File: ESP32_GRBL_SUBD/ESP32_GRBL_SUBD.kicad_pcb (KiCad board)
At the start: 2 copper layers, 67 x 91 mm, 44 parts, among them J1 DB25_Female_MountingHoles, J2 Micro_SD_Card, J3 Conn_01x19_Female, J3a1 Conn_01x19_Female, J4 Conn_01x19_Female, J4a1 Conn_01x19_Female, J5 Barrel_Jack_MountingPin, J6 Screw_Terminal_01x02, J7 Screw_Terminal_01x02, J8 Screw_Terminal_01x02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

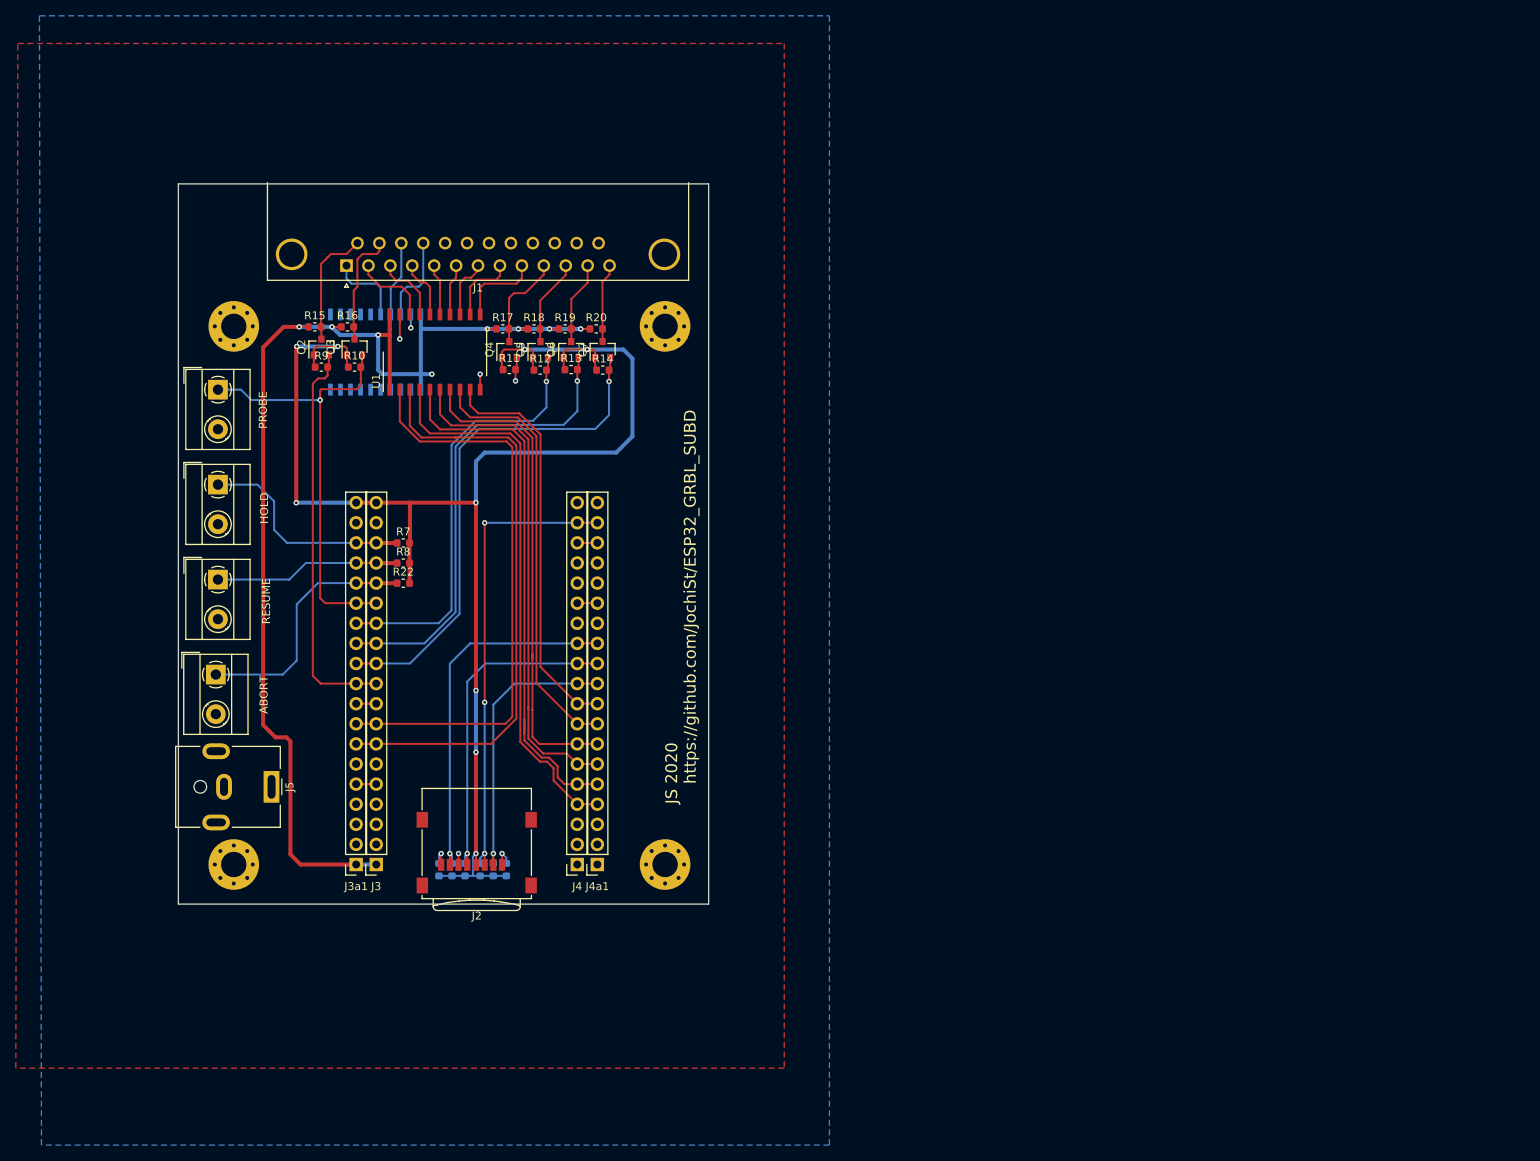
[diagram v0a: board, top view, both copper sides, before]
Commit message: added resistors to map outputs to different pins on SUB-D
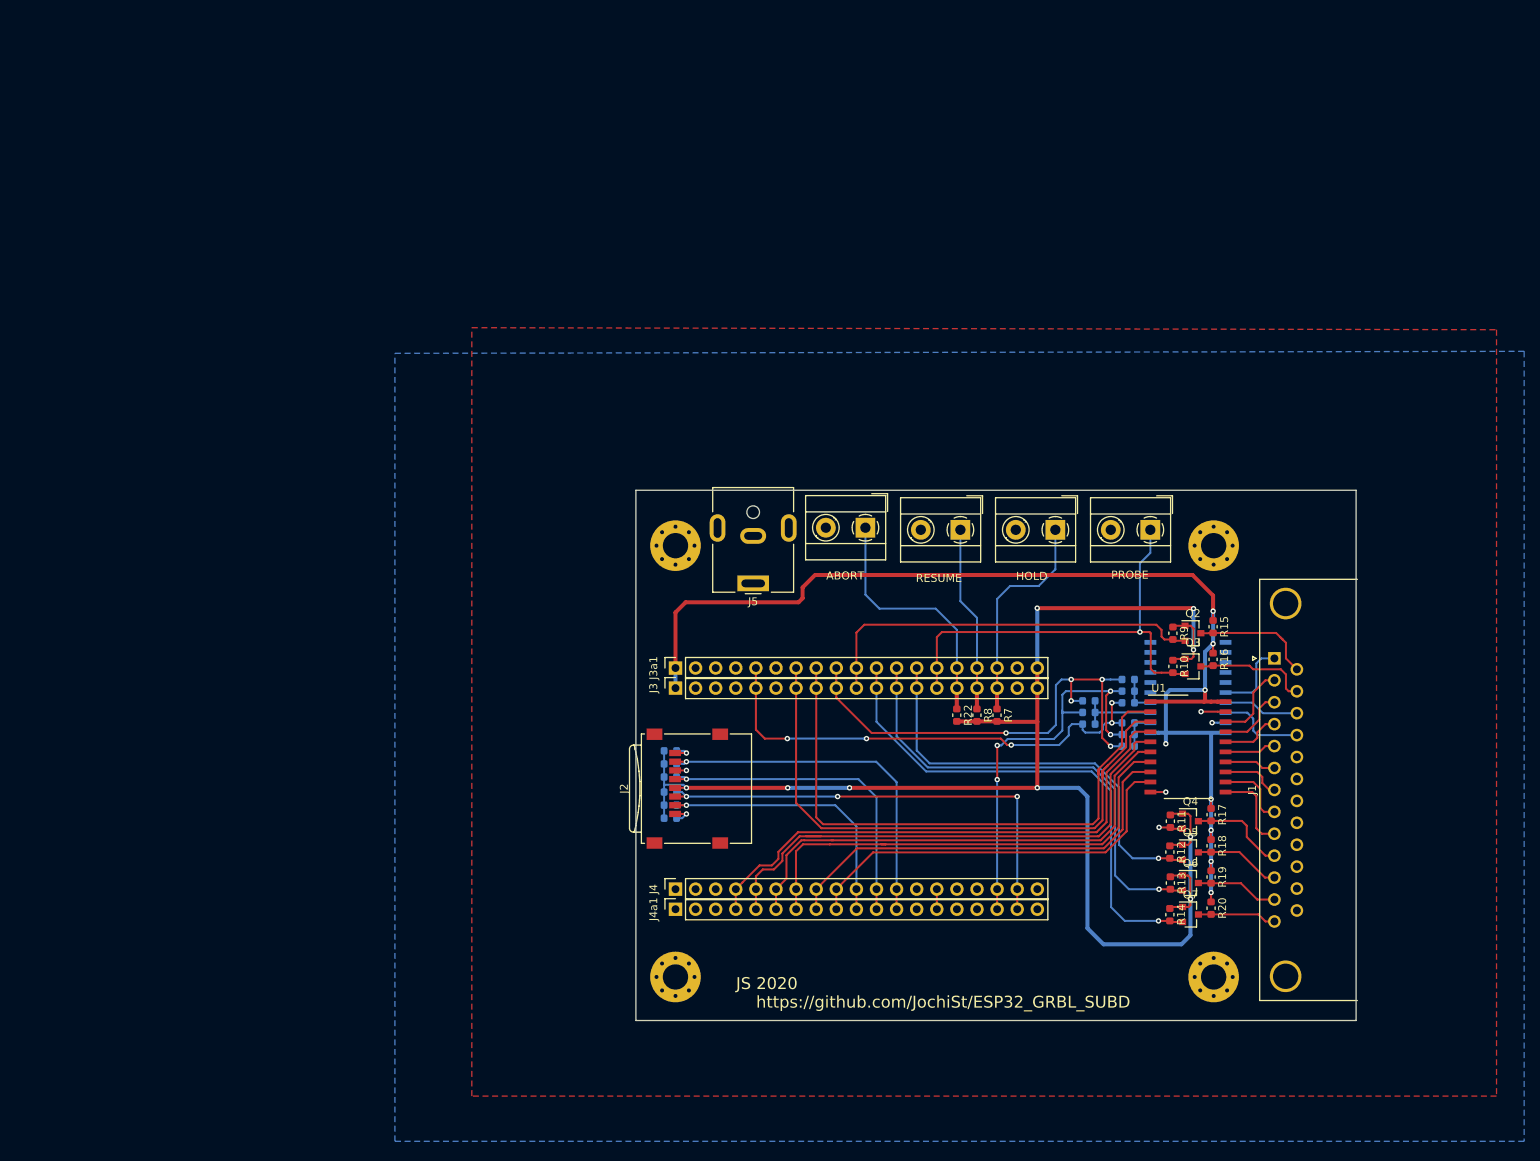
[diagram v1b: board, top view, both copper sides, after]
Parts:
- added R21: 0R, Resistor_SMD:R_0603_1608Metric, B.Cu at (138.0, 96.6)
- added R23: 0R, Resistor_SMD:R_0603_1608Metric, B.Cu at (138.0, 98.1)
- added R24: 0R, Resistor_SMD:R_0603_1608Metric, B.Cu at (138.0, 99.6)
- added R25: 0R, Resistor_SMD:R_0603_1608Metric, B.Cu at (133.0, 99.3)
- added R26: 0R, Resistor_SMD:R_0603_1608Metric, B.Cu at (133.0, 100.8)
- added R27: 0R, Resistor_SMD:R_0603_1608Metric, B.Cu at (133.0, 102.3)
- added R28: 0R, Resistor_SMD:R_0603_1608Metric, B.Cu at (138.0, 105.1)
- added R29: 0R, Resistor_SMD:R_0603_1608Metric, B.Cu at (138.0, 103.6)
- added R30: 0R, Resistor_SMD:R_0603_1608Metric, B.Cu at (138.0, 102.1)
- moved J1 127.3 mm to (156.5, 94.0), turned to 90 degrees
- moved H3 126.9 mm to (148.8, 79.7), turned to 270 degrees
- moved R15 119.7 mm to (148.7, 90.0), turned to 270 degrees
- moved J6 119.1 mm to (140.8, 77.7), turned to 180 degrees
- moved R16 117.2 mm to (148.7, 94.1), turned to 270 degrees
- moved Q2 115.9 mm to (146.2, 90.8), turned to 0 degrees
- moved Q3 113.4 mm to (146.2, 95.0), turned to 0 degrees
- moved R9 112.7 mm to (143.7, 90.8), turned to 270 degrees
- moved U2 111.1 mm to (145.6, 97.6), turned to 0 degrees
- moved R10 110.1 mm to (143.7, 95.0), turned to 270 degrees
- moved R17 108.5 mm to (148.5, 113.7), turned to 270 degrees
- moved R18 107.6 mm to (148.5, 117.6), turned to 270 degrees
- moved H2 107.5 mm to (148.8, 134.2), turned to 270 degrees
- moved U1 107.4 mm to (145.6, 105.1), turned to 0 degrees
- moved R19 107.0 mm to (148.5, 121.6), turned to 270 degrees
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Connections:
- U2 pad 5: Net-(U2-Pad5) -> GND
- U2 pad 6: Net-(U2-Pad6) -> GND
- U2 pad 7: Net-(U2-Pad7) -> GND
- U2 pad 8: /MIST_3V3 -> GND
- U2 pad 9: /FLOOD_3V3 -> GND
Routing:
- net /COOLANT_3V3: track 2.54 -> 62.1 mm, vias 0 -> 5
- net /STEP_ENABLE: track 2.54 -> 62.0 mm, vias 0 -> 5
- net /Spindle_EN_3V3: track 2.54 -> 51.9 mm, vias 0 -> 4
- net /ENABLE_3V3: track 0.00 -> 9.93 mm
- net /OUT2_3V3: track 0.00 -> 4.96 mm
- net /OUT1_3V3: track 0.00 -> 4.96 mm
- net /Y_DIR_3V3: track 69.6 -> 68.3 mm
- net /Y_STEP_3V3: track 68.9 -> 67.7 mm
- net /Z_DIR_3V3: track 63.7 -> 62.7 mm
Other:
- board size 67 x 91 mm -> 91 x 67 mm

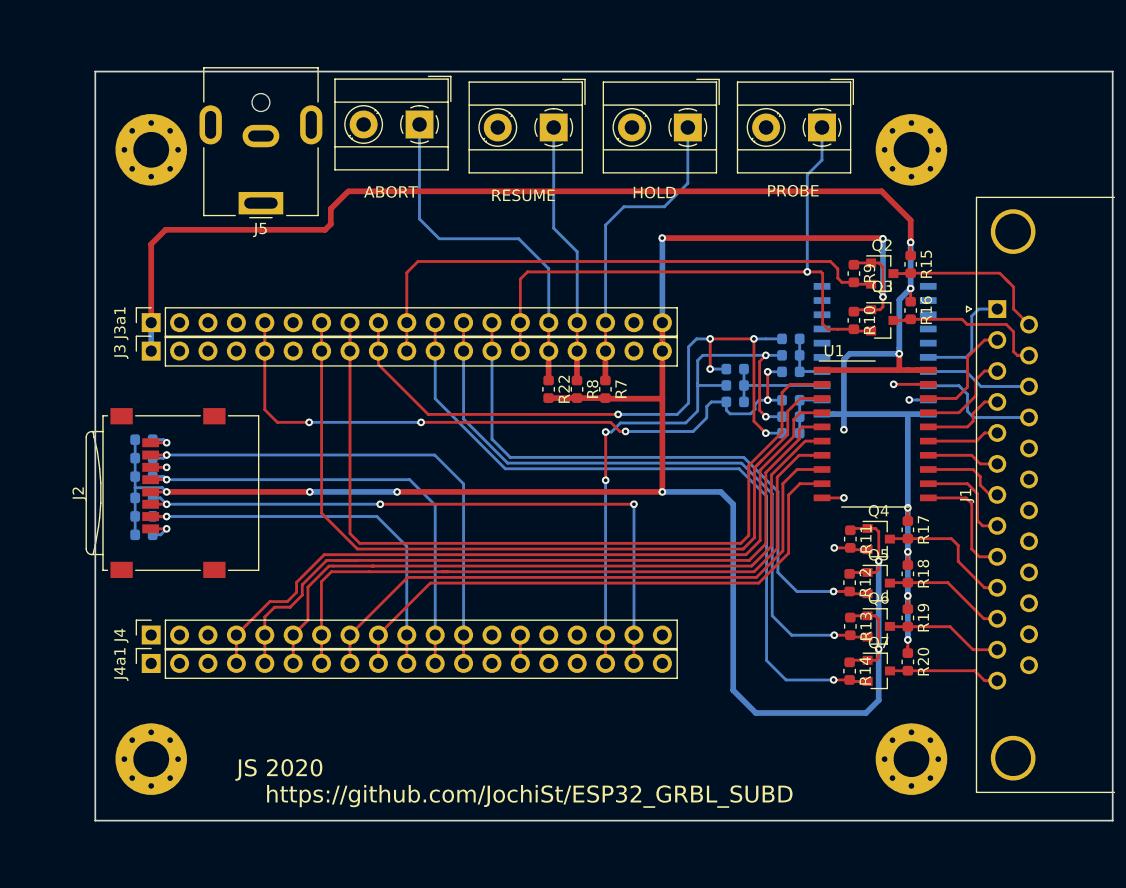
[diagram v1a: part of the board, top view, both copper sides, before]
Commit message: added level converter for outputs and some LEDs for limit switches
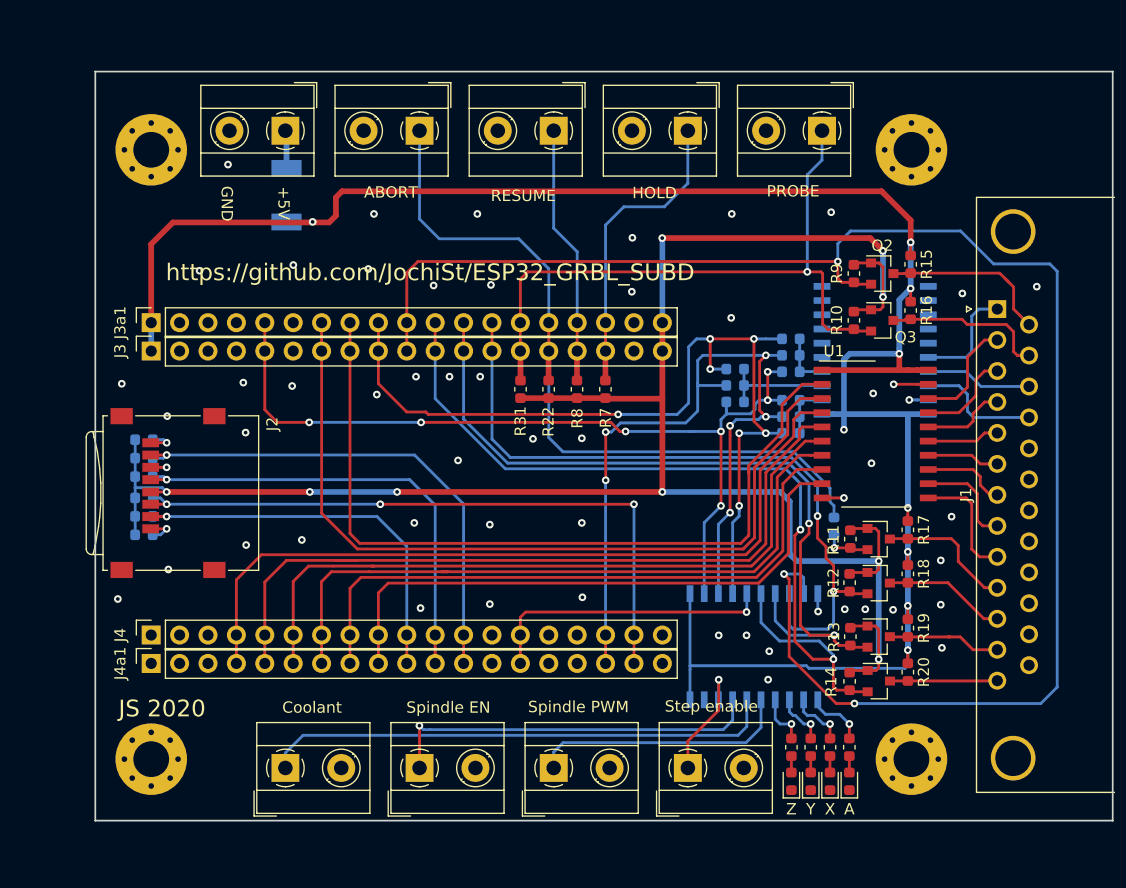
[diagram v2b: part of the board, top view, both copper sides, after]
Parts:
- added D1: SM4007, Diode_SMD:D_MELF, B.Cu at (92.9, 83.8)
- added D2: LED, LED_SMD:LED_0603_1608Metric, F.Cu at (143.3, 136.2)
- added D3: LED, LED_SMD:LED_0603_1608Metric, F.Cu at (141.5, 136.2)
- added D4: LED, LED_SMD:LED_0603_1608Metric, F.Cu at (139.8, 136.2)
- added D5: LED, LED_SMD:LED_0603_1608Metric, F.Cu at (138.1, 136.2)
- added J10: Screw_Terminal_01x02, TerminalBlock_MetzConnect:TerminalBlock_MetzConnect_Type055_RT01502HDWU_1x02_P5.00mm_Horizontal, F.Cu at (128.8, 135.0)
- added J11: Screw_Terminal_01x02, TerminalBlock_MetzConnect:TerminalBlock_MetzConnect_Type055_RT01502HDWU_1x02_P5.00mm_Horizontal, F.Cu at (104.8, 135.0)
- added J12: Screw_Terminal_01x02, TerminalBlock_MetzConnect:TerminalBlock_MetzConnect_Type055_RT01502HDWU_1x02_P5.00mm_Horizontal, F.Cu at (92.8, 135.0)
- added J13: Screw_Terminal_01x02, TerminalBlock_MetzConnect:TerminalBlock_MetzConnect_Type055_RT01502HDWU_1x02_P5.00mm_Horizontal, F.Cu at (116.8, 135.0)
- added R31: 47k, Resistor_SMD:R_0603_1608Metric, F.Cu at (113.8, 101.1)
- added R32: 0R, Resistor_SMD:R_0603_1608Metric, B.Cu at (141.9, 113.4)
- added R33: 2k7, Resistor_SMD:R_0603_1608Metric, F.Cu at (143.3, 133.1)
- added R35: 2k7, Resistor_SMD:R_0603_1608Metric, F.Cu at (139.8, 133.1)
- added R36: 2k7, Resistor_SMD:R_0603_1608Metric, F.Cu at (138.1, 133.1)
- added Re: 2k7, Resistor_SMD:R_0603_1608Metric, F.Cu at (141.5, 133.1)
- added U3: 74HCT245, Package_SO:SO-20_12.8x7.5mm_P1.27mm, B.Cu at (134.7, 124.2)
- J5: value Barrel_Jack_MountingPin -> Screw_Terminal_01x02; footprint Connector_BarrelJack:BarrelJack_CUI_PJ-063AH_Horizontal -> TerminalBlock_MetzConnect:TerminalBlock_MetzConnect_Type055_RT01502HDWU_1x02_P5.00mm_Horizontal
- moved J5 6.84 mm to (92.8, 78.0)
- moved Q6 0.91 mm to (145.9, 123.3)
- moved Q7 0.91 mm to (145.9, 127.2)
- moved R13 0.91 mm to (143.3, 123.3)
- moved R14 0.91 mm to (143.3, 127.3)
- moved R19 0.91 mm to (148.5, 122.5)
- moved R20 0.91 mm to (148.5, 126.4)
- moved J9 0.56 mm to (104.8, 78.0)
- moved J6 0.29 mm to (140.8, 78.0)
- moved J7 0.29 mm to (128.8, 78.0)
- moved J8 0.29 mm to (116.8, 78.0)
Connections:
- net /Spindle_PWM_3V renamed /Spindle_PWM_3V3
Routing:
- net /A_LIM_3V3: track 50.3 -> 148.2 mm, vias 0 -> 3
- net /COOLANT_5V: track 0.00 -> 46.0 mm
- net /ABORT: track 31.9 -> 69.4 mm
- net /SPINDLE_EN_5V: track 0.00 -> 34.1 mm, vias 0 -> 1
- net +5V: track 153.7 -> 186.7 mm, vias 8 -> 9
- net /Spindle_PWM_3V3: track 2.54 -> 26.9 mm, vias 0 -> 1
- net /SPINDLE_PWM_5V: track 0.00 -> 23.4 mm
- net /Spindle_EN_3V3: track 51.9 -> 71.1 mm, vias 4 -> 6
- net /COOLANT_3V3: track 62.1 -> 80.0 mm, vias 5 -> 7
- net /STEP_ENABLE: track 62.0 -> 77.6 mm, vias 5 -> 7
- net +3V3: track 194.9 -> 180.0 mm
- net /Z_LIM_3V3: track 64.6 -> 77.4 mm, vias 1 -> 2
- net /Y_LIM_3V3: track 59.2 -> 70.3 mm, vias 1 -> 2
- net /STEP_EN_5V: track 0.00 -> 10.9 mm, vias 0 -> 1
- net /X_LIM_3V3: track 54.0 -> 64.5 mm, vias 1 -> 2
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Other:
- board text added: "+5V"
- board text added: "A"
- board text added: "Coolant"
- board text added: "GND"
- board text added: "Spindle EN"
- board text added: "Spindle PWM"
- board text added: "Step enable"
- board text added: "X"
- board text added: "Y"
- board text added: "Z"

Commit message: added decoupling Cs
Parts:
- added C1: 100n, Capacitor_SMD:C_0603_1608Metric, B.Cu at (152.2, 102.8)
- added C2: 100n, Capacitor_SMD:C_0603_1608Metric, F.Cu at (81.6, 92.6)
- added C3: 100n, Capacitor_SMD:C_0603_1608Metric, B.Cu at (129.6, 130.7)
- added C4: 100n, Capacitor_SMD:C_0603_1608Metric, F.Cu at (152.1, 100.1)
- added C5: 1u, Capacitor_SMD:C_0603_1608Metric, B.Cu at (83.7, 109.5)
- added C6: 100n, Capacitor_SMD:C_0603_1608Metric, B.Cu at (85.3, 109.5)
- added C7: 100n, Capacitor_SMD:C_0603_1608Metric, F.Cu at (127.3, 100.6)
- renumbered Re to R34
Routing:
- net +5V: track 186.7 -> 193.3 mm
- net GND: track 9.80 -> 13.9 mm, vias 55 -> 62
- net /SD_CLK: vias 1 -> 2
- net +3V3: vias 9 -> 8

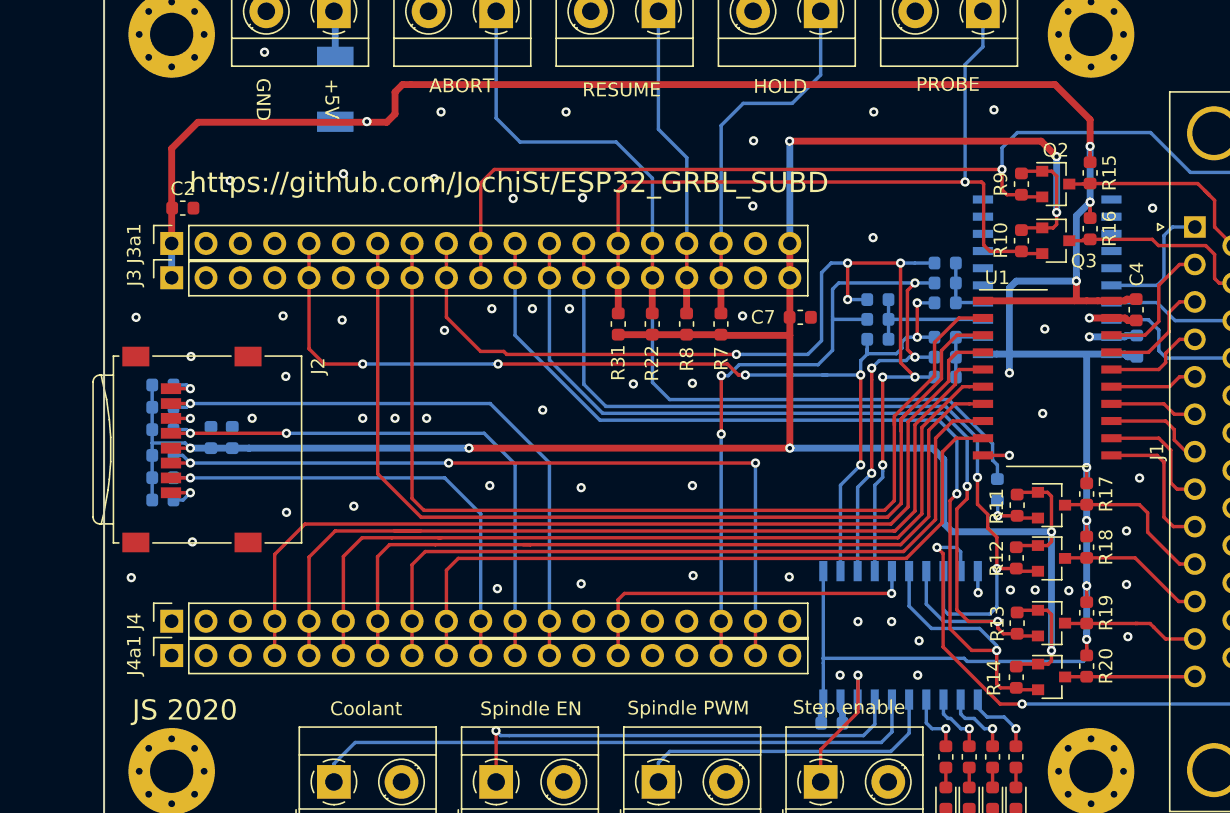
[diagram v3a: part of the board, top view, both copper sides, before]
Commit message: some cleanup and connections of U0RX / TX and EN to second pin header
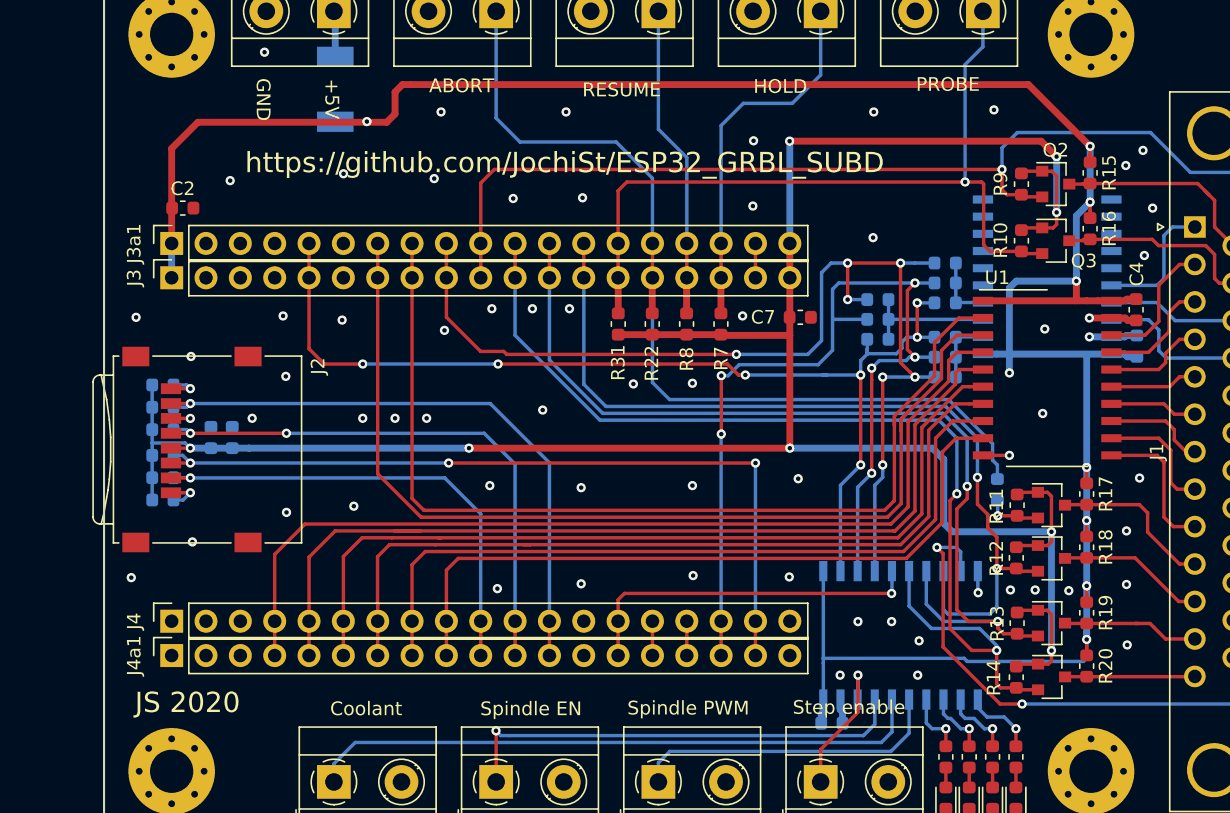
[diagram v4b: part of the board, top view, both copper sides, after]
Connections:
- J3 pad 18: Net-(J3-Pad18) -> /EN
- J3a1 pad 18: Net-(J3a1-Pad18) -> /EN
- J4 pad 15: Net-(J4-Pad15) -> /U0RX
- J4 pad 16: Net-(J4-Pad16) -> /U0TX
- J4a1 pad 15: Net-(J4a1-Pad15) -> /U0RX
- J4a1 pad 16: Net-(J4a1-Pad16) -> /U0TX
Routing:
- net /U0TX: track 0.00 -> 2.54 mm
- net /U0RX: track 0.00 -> 2.54 mm
- net /EN: track 0.00 -> 2.54 mm
- net +5V: track 193.3 -> 192.1 mm
- net GND: vias 62 -> 66

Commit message: added placement variant of first version
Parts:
- R23, R24, R25, R26, R27, R28, R30, R32: value 0R -> dnp
